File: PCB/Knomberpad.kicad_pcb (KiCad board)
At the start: 2 copper layers, 99.2 x 95.3 mm, 38 parts, among them SW1 Rotary_Encoder, U1 ProMicro

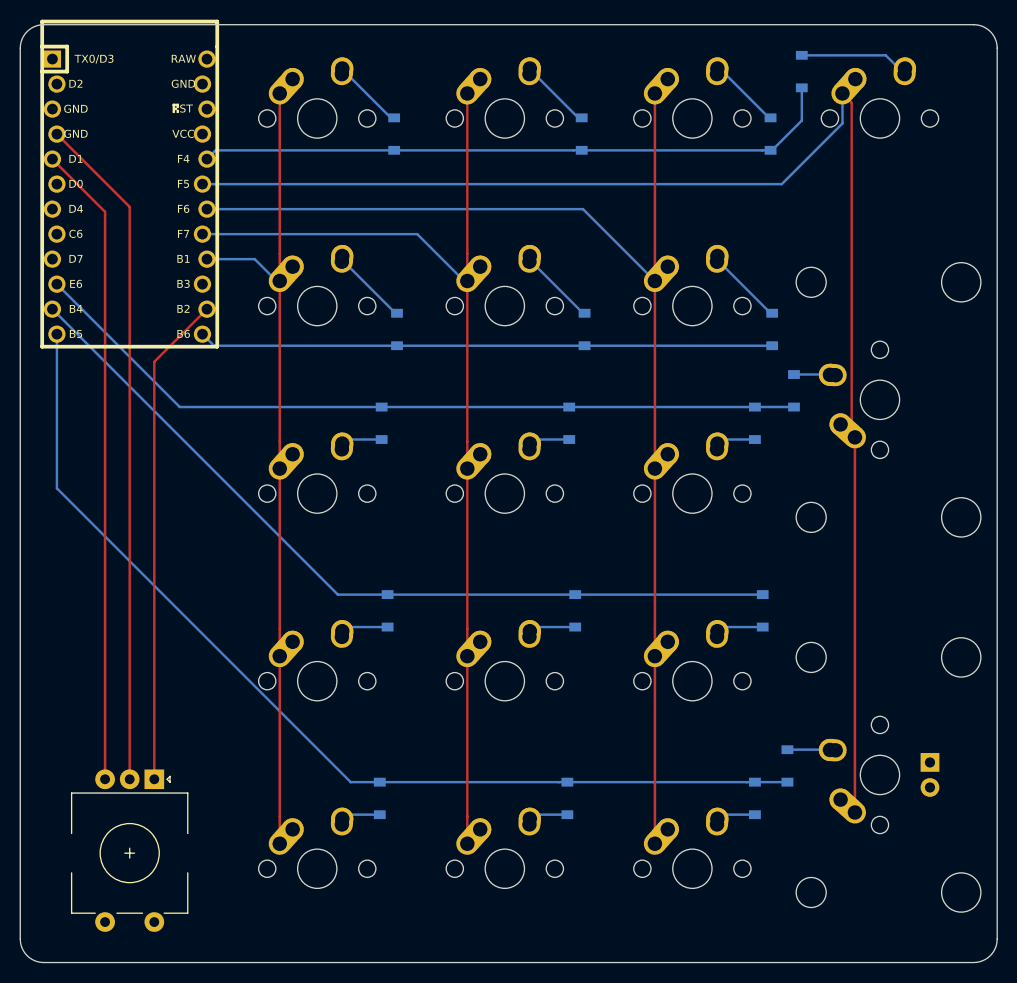
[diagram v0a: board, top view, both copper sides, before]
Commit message: Change footprints
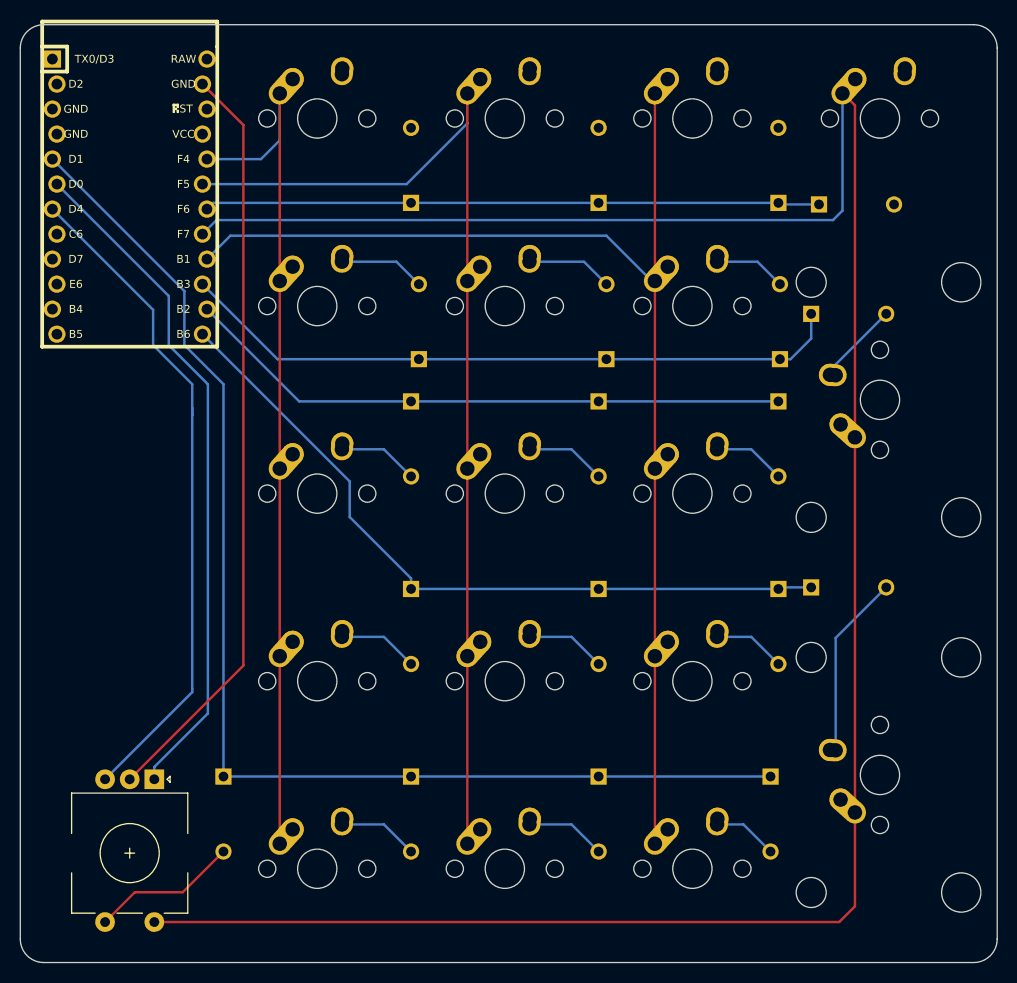
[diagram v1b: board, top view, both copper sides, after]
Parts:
- added D19: D_Small, keebio:Diode, B.Cu at (59.5, 119.1)
- D1, D12, D13, D14, D2, D3, D4, D5, D6, D7: footprint ai03:D_SOD-123-Pretty -> keebio:Diode
- D10: renamed from D9; footprint ai03:D_SOD-123-Pretty -> keebio:Diode
- D11: renamed from D10; footprint ai03:D_SOD-123-Pretty -> keebio:Diode
- D15: renamed from D18; footprint ai03:D_SOD-123-Pretty -> keebio:Diode
- D16: renamed from D15; footprint ai03:D_SOD-123-Pretty -> keebio:Diode
- D17: renamed from D16; footprint ai03:D_SOD-123-Pretty -> keebio:Diode
- D18: renamed from D17; footprint ai03:D_SOD-123-Pretty -> keebio:Diode
- D8: renamed from D11; footprint ai03:D_SOD-123-Pretty -> keebio:Diode
- D9: renamed from D8; footprint ai03:D_SOD-123-Pretty -> keebio:Diode
- MX15: renamed from MX18; footprint ai03_switch:MX-2U -> ai03_switch:MX-2U-NoLED
- SW19: renamed from SW1; value Rotary_Encoder -> RT1
- moved D15 19.2 mm to (123.0, 96.0), turned to 180 degrees
- moved D4 14.6 mm to (123.8, 57.1), turned to 180 degrees
- moved D8 9.59 mm to (123.0, 68.3), turned to 180 degrees
- moved D1 3.61 mm to (78.6, 53.2), turned to 270 degrees
- moved D2 3.61 mm to (97.6, 53.2), turned to 270 degrees
- moved D16 3.55 mm to (78.6, 119.1), turned to 90 degrees
- moved D17 3.55 mm to (97.6, 119.1), turned to 90 degrees
- moved D10 3.38 mm to (97.6, 81.0), turned to 90 degrees
- moved D9 3.38 mm to (78.6, 81.0), turned to 90 degrees
- moved D3 3.27 mm to (115.9, 53.2), turned to 270 degrees
- moved D11 2.86 mm to (115.9, 81.0), turned to 90 degrees
- moved D12 2.86 mm to (78.6, 100.0), turned to 90 degrees
- moved D13 2.86 mm to (97.6, 100.0), turned to 90 degrees
- moved D5 2.36 mm to (79.4, 69.1), turned to 270 degrees
- moved D6 2.36 mm to (98.4, 69.1), turned to 270 degrees
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- renumbered MX9 to MX10, MX10 to MX11, MX15 to MX16, MX16 to MX17, MX17 to MX18, MX11 to MX8, MX8 to MX9
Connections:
- D15 pad 1: ROW4 -> ROW3
- D8 pad 1: ROW2 -> ROW1
- SW19 pad S1: (no net) -> Net-(D19-Pad2)
- SW19 pad S2: (no net) -> COL3
- U1 pad 10: ROW2 -> Net-(U1-Pad10)
- U1 pad 11: ROW3 -> Net-(U1-Pad11)
- U1 pad 12: ROW4 -> Net-(U1-Pad12)
- U1 pad 13: ROW1 -> ROW3
- U1 pad 14: ROT_A -> ROW2
- U1 pad 15: Net-(U1-Pad15) -> ROW1
- U1 pad 16: COL0 -> COL2
- U1 pad 17: COL1 -> COL3
- U1 pad 18: COL2 -> ROW0
- U1 pad 19: COL3 -> COL1
- U1 pad 20: ROW0 -> COL0
- U1 pad 23: Net-(U1-Pad23) -> ROT_C
- U1 pad 4: ROT_C -> Net-(U1-Pad4)
- U1 pad 5: ROT_B -> ROW4
- U1 pad 6: Net-(U1-Pad6) -> ROT_A
- U1 pad 7: Net-(U1-Pad7) -> ROT_B
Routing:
- net COL3: track 144.1 -> 232.8 mm
- net ROW4: track 102.2 -> 125.5 mm
- net ROT_A: track 50.0 -> 69.0 mm
- net ROW2: track 80.0 -> 61.9 mm
- net Net-(D19-Pad2): track 0.00 -> 15.1 mm
- net Net-(D15-Pad2): track 4.93 -> 18.7 mm
- net Net-(D4-Pad2): track 12.5 -> 0.73 mm
- net ROW1: track 58.3 -> 68.4 mm
- net ROW3: track 84.1 -> 75.4 mm
- net ROT_C: track 68.6 -> 77.1 mm
- net Net-(D3-Pad2): track 7.31 -> 0.98 mm
- net Net-(D2-Pad2): track 7.23 -> 0.98 mm
- net Net-(D1-Pad2): track 7.23 -> 0.98 mm
- net COL0: track 84.5 -> 89.1 mm
- net Net-(D8-Pad2): track 4.26 -> 8.36 mm
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
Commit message: add branding and gerbers
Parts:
- added  : MountingHole_3.2mm_M3, MountingHole:MountingHole_3.2mm_M3, B.Cu at (127.8, 126.2)
- added  : MountingHole_3.2mm_M3, MountingHole:MountingHole_3.2mm_M3, B.Cu at (50.8, 105.6)
- added G***: LOGO, djlee_art:Fish_Cu, F.Cu at (50.8, 87.3)
- added G***: LOGO, djlee_art:Fish_Mask, F.Cu at (50.8, 87.3)
- added G***: LOGO, djlee_art:KnomberPadLogo, B.Cu at (42.9, 94.5)
- added REF**: , MountingHole:MountingHole_3.2mm_M3, B.Cu at (131.8, 59.5)
- moved D4 0.79 mm to (123.0, 57.1)
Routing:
- net Net-(D4-Pad2): track 0.73 -> 15.3 mm
- net Net-(D2-Pad2): track 0.98 -> 10.3 mm
- net Net-(D1-Pad2): track 0.98 -> 10.3 mm
- net Net-(D3-Pad2): track 0.98 -> 9.47 mm
- net ROT_B: track 68.2 -> 67.5 mm
- net ROW0: track 62.5 -> 61.7 mm
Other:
- board text added: "Rev 2.0.0"
- board text added: "djlee.xyz"
- board text added: "https://github.com/davidjameslee/knomberpad"
